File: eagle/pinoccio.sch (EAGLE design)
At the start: 51 parts, among them Q1 16MHz, Q2 32.768k, Q4 MOSFET-PCHANNEL, Q5 TRANSISTOR-NPN-DUAL, U1 MCP73831, U2 3.3V, U4 ATMEGA128RFA1, X1 USB-MICROB, Y2 ANTENNA2SMD5

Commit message: Update licensing on eagle files
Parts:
- removed U$3: CREATIVE_COMMONS, SparkFun:CREATIVE_COMMONS
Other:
- note added: "0.5"
- note added: "Copyright Pinoccio 2012"
- note added: "INCLUDING OF MERCHANTABILITY, SATISFACTORY QUALITY AND FITNESS FOR A"
- note added: "PARTICULAR PURPOSE. Please see the CERN OHL v.1.1 for applicable conditions"
- note added: "This documentation describes Open Hardware and is licensed under"
- note added: "This documentation is distributed WITHOUT ANY EXPRESS OR IMPLIED WARRANTY,"
- note added: "the CERN OHL v. 1.1. You may redistribute and modify this documentation"
- note added: "under the terms of the CERN OHL v.1.1. (http://ohwr.org/cernohl)."
- note removed: "0.6"
- note removed: "Eric Jennings for Pinoccio"
- note removed: "Portions based on Arduino Fio and SparkFun ATMega128rfa1 breakout board"
- moved on the sheet: B1, C1, C10, C9, Q4, Q5, R1, R5, R6, R7, Y2

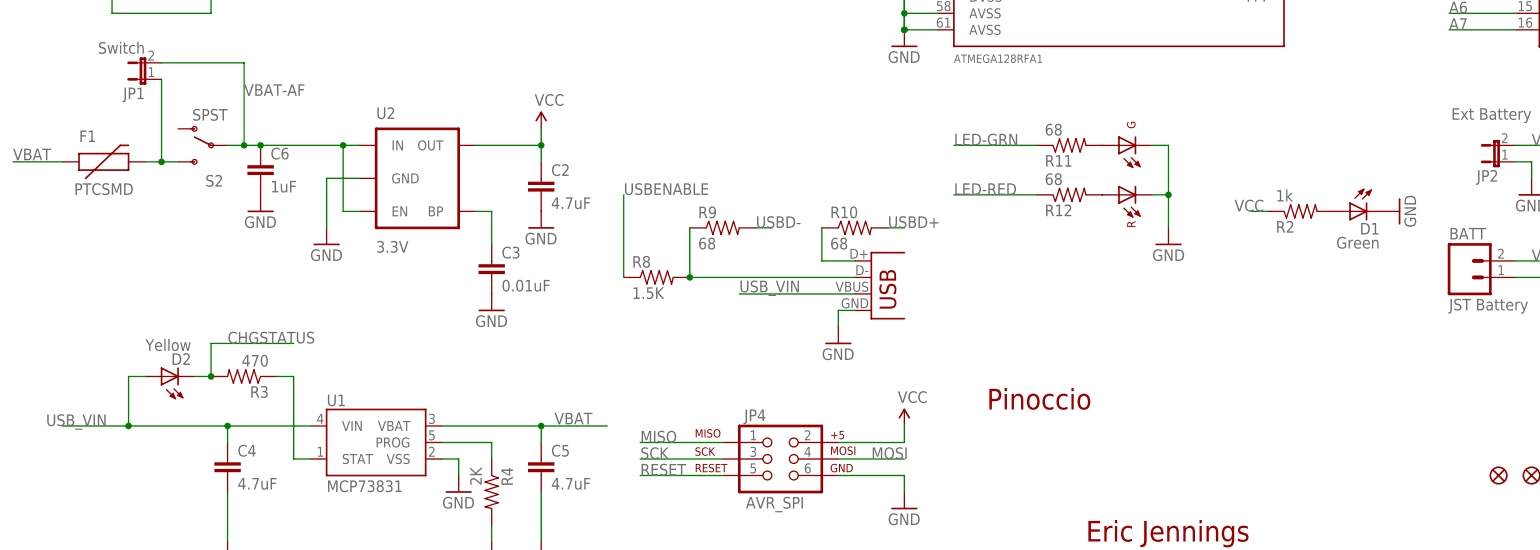
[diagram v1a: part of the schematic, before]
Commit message: Removed D1 LED for power--for better power handling.  Instead, will modify the bootloader to flash the bicolor LED a couple times upon power up, then turn off.  Thanks Louis for the idea!
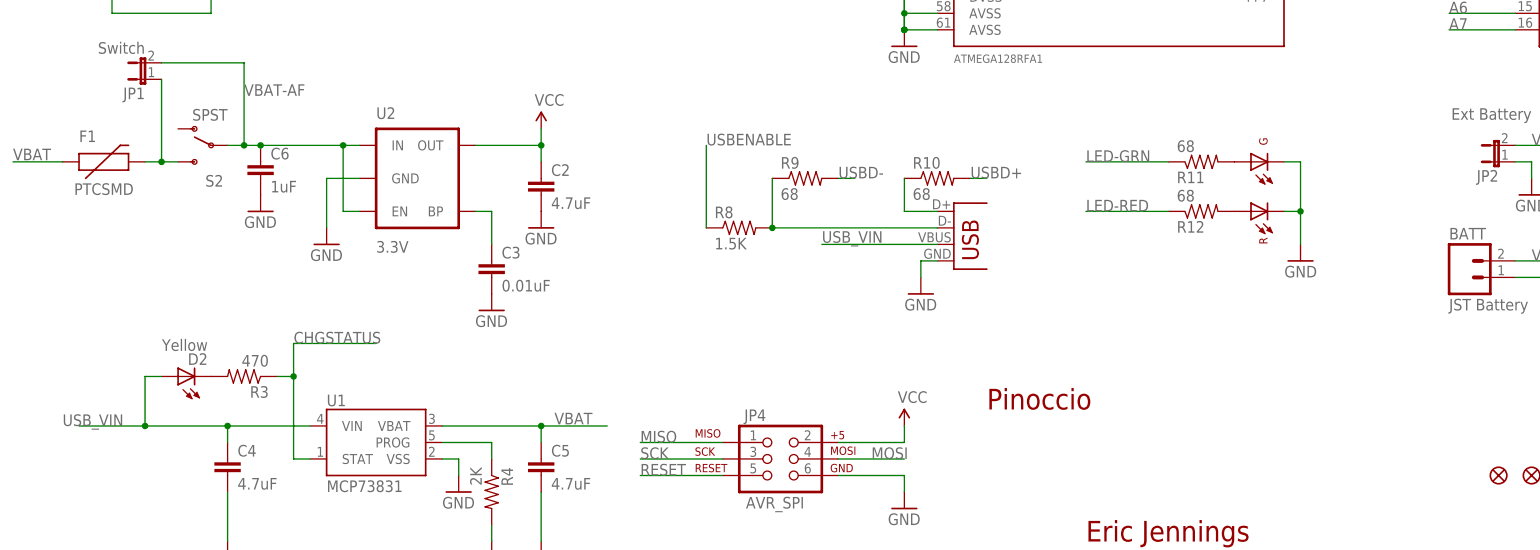
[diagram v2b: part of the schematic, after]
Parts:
- removed D1: Green, SparkFun:LED0603
- removed R2: 1k, SparkFun:RESISTOR0402-RES
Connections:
- removed net N$14: R3.1, U1.STAT
- net CHGSTATUS: now also R3.1, U1.STAT; no longer D2.C, R3.2
- net GND: no longer D1.C
- net N$22: now also D2.C, R3.2; no longer D1.A, R2.2
- net VCC: no longer R2.1
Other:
- moved on the sheet: D2, R10, R11, R12, R8, R9

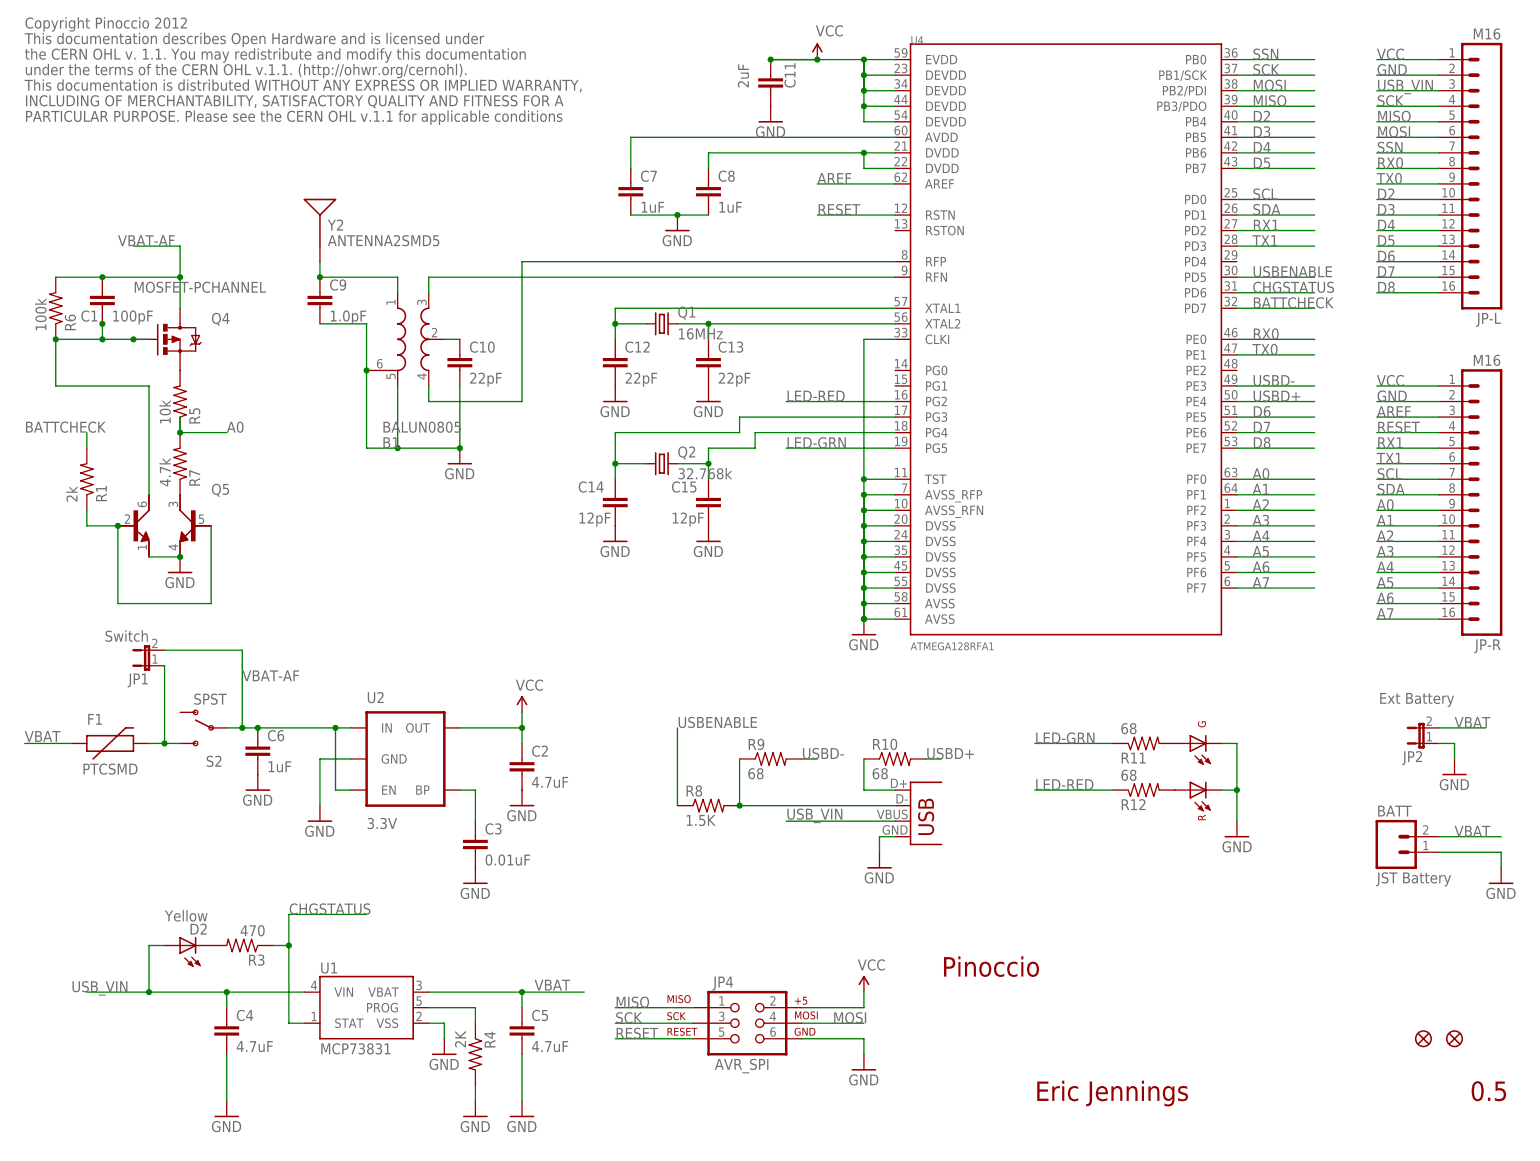
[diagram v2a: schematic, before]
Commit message: Updated bicolor LED values to a more sane value.  Add 0603 landing pattern for Lipo IC charge current capacity (for people to mod if they want higher C-ratings).  Fix mosfet reversal error.  (Thanks Monty!)
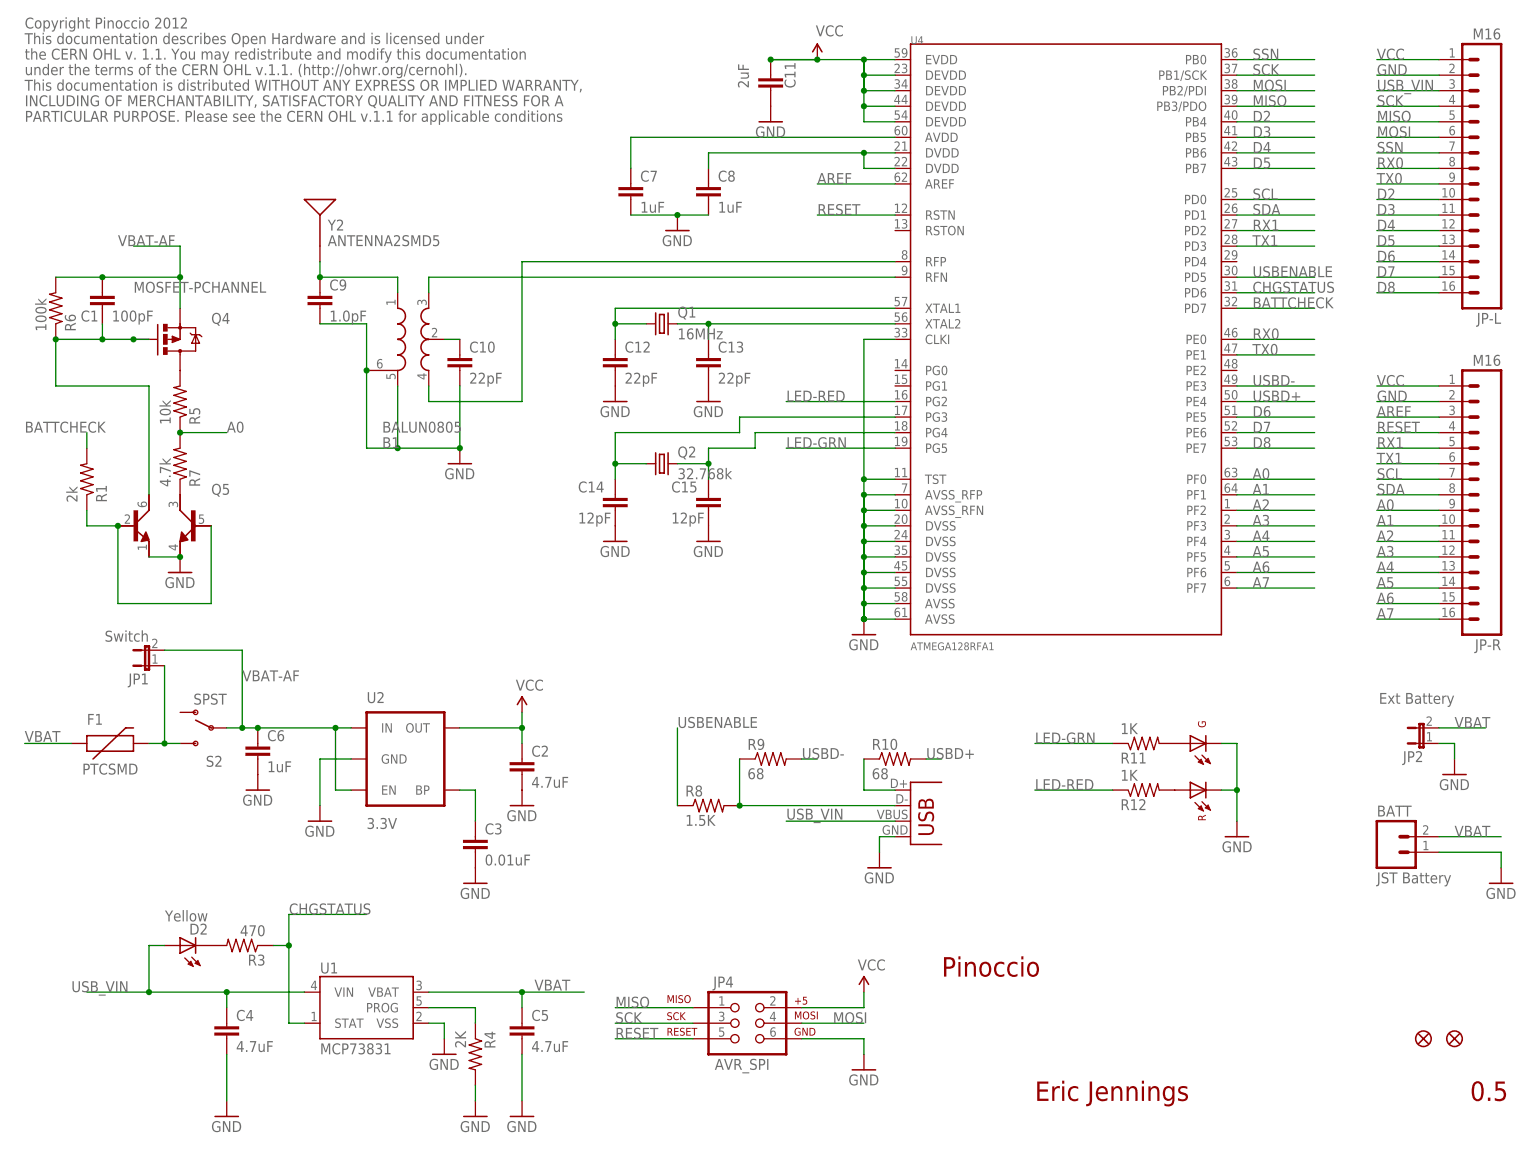
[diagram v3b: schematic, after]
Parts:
- Q4: device SparkFun:MOSFET-PCHANNELSMD -> Pinoccio:MOSFET-PCHANNELSMD
- R11, R12: value 68 -> 1K
- R4: device SparkFun:RESISTOR0402-RES -> SparkFun:RESISTOR0603-RES
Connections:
- net N$3: now also Q4.D; no longer Q4.S
- net VBAT-AF: now also Q4.S; no longer Q4.D
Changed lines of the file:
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@@
 <part name="U$5" library="SparkFun" deviceset="FIDUCIAL" device="1X2"/>
 <part name="U1" library="SparkFun" deviceset="MCP73831" device="SMD" value="MCP73831"/>
-<part name="R4" library="SparkFun" deviceset="RESISTOR" device="0402-RES" value="2K"/>
+<part name="R4" library="SparkFun" deviceset="RESISTOR" device="0603-RES" value="2K"/>
 <part name="GND14" library="supply1" deviceset="GND" device=""/>
 <part name="GND17" library="supply1" deviceset="GND" device=""/>
@@
 <part name="R7" library="SparkFun" deviceset="RESISTOR" device="0402-RES" value="4.7k"/>
 <part name="C1" library="SparkFun" deviceset="CAP" device="0402-CAP" value="100pF"/>
-<part name="Q4" library="SparkFun" deviceset="MOSFET-PCHANNEL" device="SMD" value="MOSFET-PCHANNEL"/>
+<part name="Q4" library="Pinoccio" deviceset="MOSFET-PCHANNEL" device="SMD" value="MOSFET-PCHANNEL"/>
 <part name="GND6" library="SparkFun" deviceset="GND" device=""/>
 <part name="R1" library="SparkFun" deviceset="RESISTOR" device="0402-RES" value="2k"/>
@@
 <part name="JP1" library="Pinoccio" deviceset="JUMPER-2" device="PTH" value="Switch"/>
 <part name="JP2" library="Pinoccio" deviceset="JUMPER-2" device="PTH" value="Ext Battery"/>
-<part name="R11" library="SparkFun" deviceset="RESISTOR" device="0402-RES" value="68"/>
+<part name="R11" library="SparkFun" deviceset="RESISTOR" device="0402-RES" value="1K"/>
 <part name="GND13" library="SparkFun" deviceset="GND" device=""/>
-<part name="R12" library="SparkFun" deviceset="RESISTOR" device="0402-RES" value="68"/>
+<part name="R12" library="SparkFun" deviceset="RESISTOR" device="0402-RES" value="1K"/>
 <part name="U$1" library="Pinoccio" deviceset="LED-BICOLOR" device=""/>
 <part name="Q5" library="Pinoccio" deviceset="TRANSISTOR-NPN-DUAL" device=""/>
@@
 <net name="VBAT-AF" class="0">
 <segment>
-<pinref part="Q4" gate="G$1" pin="D"/>
-<wire x1="27.94" y1="137.16" x2="27.94" y2="142.24" width="0.1524" layer="91"/>
 <wire x1="27.94" y1="142.24" x2="27.94" y2="147.32" width="0.1524" layer="91"/>
 <wire x1="27.94" y1="147.32" x2="20.32" y2="147.32" width="0.1524" layer="91"/>
@@
 <pinref part="C1" gate="G$1" pin="1"/>
 <wire x1="27.94" y1="142.24" x2="15.24" y2="142.24" width="0.1524" layer="91"/>
-<junction x="27.94" y="142.24"/>
 <junction x="15.24" y="142.24"/>
+<pinref part="Q4" gate="G$1" pin="S"/>
+<wire x1="27.94" y1="137.16" x2="27.94" y2="142.24" width="0.1524" layer="91"/>
+<junction x="27.94" y="142.24"/>
 </segment>
 <segment>
@@
 </segment>
 <segment>
-<wire x1="27.94" y1="119.38" x2="27.94" y2="116.84" width="0.1524" layer="91"/>
 <pinref part="R5" gate="G$1" pin="1"/>
 <pinref part="R7" gate="G$1" pin="2"/>
@@
 <wire x1="20.32" y1="132.08" x2="22.86" y2="132.08" width="0.1524" layer="91"/>
 <junction x="20.32" y="132.08"/>
-<junction x="15.24" y="134.62"/>
 <junction x="7.62" y="132.08"/>
 <junction x="15.24" y="132.08"/>
@@
 </segment>
 </net>
-<net name="N$3" class="0">
-<segment>
-<pinref part="Q4" gate="G$1" pin="S"/>
-<pinref part="R5" gate="G$1" pin="2"/>
-</segment>
-</net>
 <net name="BATTCHECK" class="0">
 <segment>
@@
 </segment>
 </net>
+<net name="N$3" class="0">
+<segment>
+<pinref part="Q4" gate="G$1" pin="D"/>
+<pinref part="R5" gate="G$1" pin="2"/>
+</segment>
+</net>
